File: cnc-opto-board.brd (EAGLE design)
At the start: 53 x 73 mm, 25 parts, among them J1 TTL, J2 FIELD, J3 POWER, Q1 P2N2222A, Q2 P2N2222A, U1 ATTINY85

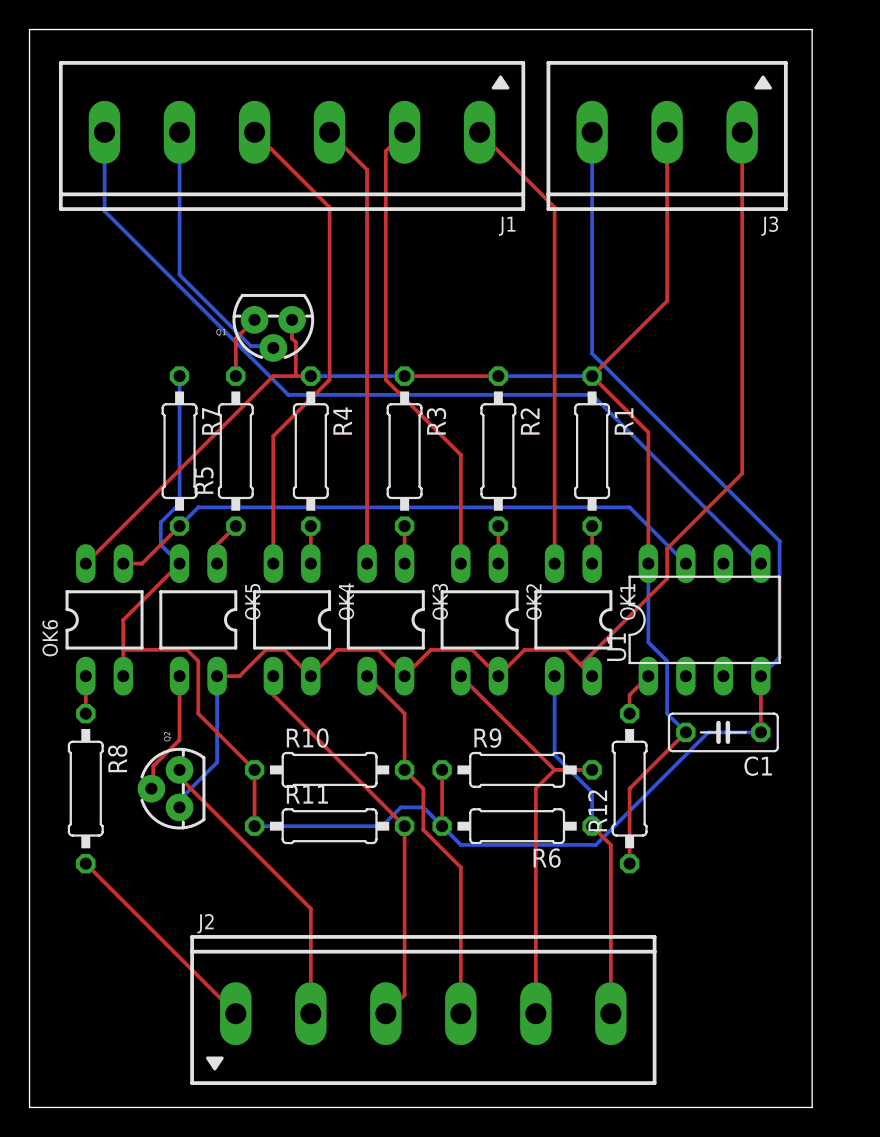
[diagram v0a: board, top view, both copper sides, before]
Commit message: UPDATE: sized board outline to fit DIN rail mount frame and routed.
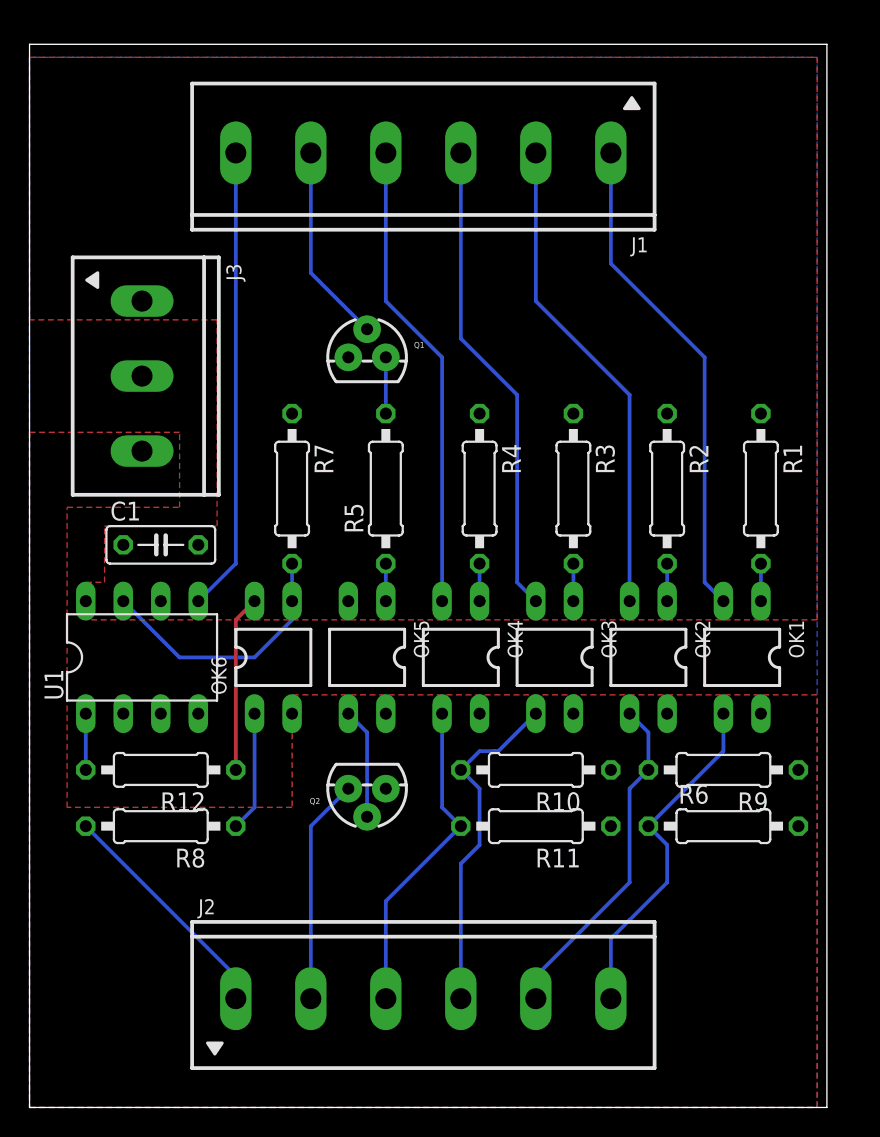
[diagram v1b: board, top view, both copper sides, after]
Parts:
- moved C1 40.2 mm to (8.89, 38.1), turned to 0 degrees
- moved J3 39.2 mm to (7.62, 49.5), turned to 270 degrees
- moved U1 38.2 mm to (7.62, 30.5)
- moved R12 31.8 mm to (8.89, 22.9), turned to 180 degrees
- moved R10 14.0 mm to (34.3, 22.9), turned to 180 degrees
- moved R11 14.0 mm to (34.3, 19.1), turned to 180 degrees
- moved R6 14.0 mm to (47.0, 19.1), turned to 0 degrees
- moved R9 14.0 mm to (47.0, 22.9), turned to 180 degrees
- moved Q2 12.7 mm to (22.9, 21.6), turned to 180 degrees
- moved OK3 11.7 mm to (35.6, 30.5)
- moved OK6 11.7 mm to (16.5, 30.5)
- moved OK1 11.7 mm to (48.3, 30.5)
- moved OK4 11.7 mm to (29.2, 30.5)
- moved OK5 11.7 mm to (22.9, 30.5)
- moved R1 11.7 mm to (49.5, 41.9)
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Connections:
- net +24V: now also J3.3; no longer J3.1
- net +5V: now also J3.1; no longer J3.2
- net GND: now also J3.2; no longer J3.3
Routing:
- net GND: track 130.4 -> 0.00 mm
- net +5V: track 99.3 -> 12.0 mm
- net +24V: track 81.8 -> 0.00 mm
- net N$10: track 59.7 -> 31.4 mm
- net ENABLE_TTL: track 41.3 -> 17.9 mm
- net N$6: track 2.54 -> 8.15 mm
- net YLIMIT: track 28.6 -> 23.0 mm
- net PROBE: track 27.1 -> 21.9 mm
- net !ESTOP_FIELD: track 20.2 -> 15.3 mm
- net N$7: track 18.1 -> 13.5 mm
- net ZLIMIT: track 25.5 -> 23.2 mm
- net !ZLIMIT: track 30.3 -> 32.5 mm
- net !XLIMIT: track 31.3 -> 33.5 mm
- net ENABLE_FIELD: track 14.4 -> 15.9 mm
- net !YLIMIT: track 31.8 -> 33.0 mm
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- added copper zone on layer 1, net +24V
- added copper zone on layer 1, net +5V
- added copper zone on layer 16, net GND
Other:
- board size 53 x 73 mm -> 54 x 72 mm

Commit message: RTM: aesthetics and shrink-wrap for the opto board, ready for tape-out.
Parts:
- added LOGO1: OSHW-LOGOL, SparkFun-Aesthetics:OSHW-LOGO-L
- R11: value 47K -> 4K7
- R5: value 680 -> 820
- R6: value 47K -> 10K
- R7: value 10K -> 47K
- R8: value 4K7 -> 47K
- moved R8 38.3 mm to (47.0, 22.9)
- moved R6 37.1 mm to (17.8, 41.9), turned to 270 degrees
- moved R7 37.1 mm to (47.0, 19.1), turned to 0 degrees
- moved R11 25.4 mm to (8.89, 19.1)
- moved J3 14.9 mm to (10.2, 64.3), turned to 180 degrees
- moved R9 12.7 mm to (34.3, 22.9)
- moved J1 8.90 mm to (35.6, 64.3)
- moved R10 3.81 mm to (34.3, 19.1)
- moved J2 0.25 mm to (26.7, 7.62)
- turned C1 to 180 degrees
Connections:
- net N$10 renamed WATCHDOG
- net ENABLE_FIELD: now also R11.2; no longer R8.2
- net ENABLE_TTL: now also R6.2; no longer R7.2
- net GND: now also R6.1, R7.2, R8.1; no longer R11.1, R6.2, R7.1
- net N$6: now also R11.1; no longer R8.1
- net PROBE: now also R10.2; no longer R11.2
- net XLIMIT: now also R7.1; no longer R6.1
- net YLIMIT: now also R8.2; no longer R9.2
- net ZLIMIT: now also R9.2; no longer R10.2
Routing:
- net +5V: track 12.0 -> 0.00 mm
- net WATCHDOG: track 31.4 -> 34.7 mm
- net !XLIMIT: track 33.5 -> 30.5 mm
- net !YLIMIT: track 33.0 -> 31.0 mm
- net XLIMIT: track 23.5 -> 22.2 mm
- net !ZLIMIT: track 32.5 -> 31.6 mm
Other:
- board text added: "!ESTP"
- board text added: "!PROB"
- board text added: "!XLIM"
- board text added: "!YLIM"
- board text added: "!ZLIM"
- board text added: "(C) 2016 Radu - Eosif Mihailescu"
- board text added: "+24V"
- board text added: "+5V"
- board text added: "20160921"
- board text added: "BOTC"
- board text added: "BOTS"
- board text added: "ENAB"
- board text added: "ESTP"
- board text added: "GND"
- board text added: "PROB"
- board text added: "TOPC"
- board text added: "TOPS"
- board text added: "WDG"
- board text added: "XLIM"
- board text added: "YLIM"
- board text added: "ZLIM"
- board text added: "https://github.com/csdexter/cnccp-pcb"
